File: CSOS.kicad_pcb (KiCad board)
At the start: 2 copper layers, 49.5 x 67.3 mm, 23 parts, among them P101 CONN_01X02, P102 CONN_01X03, P103 CONN_01X02, P201 CONN_01X01, Q201 BUK9575, U201 LMV358, U401 LM2931D-R

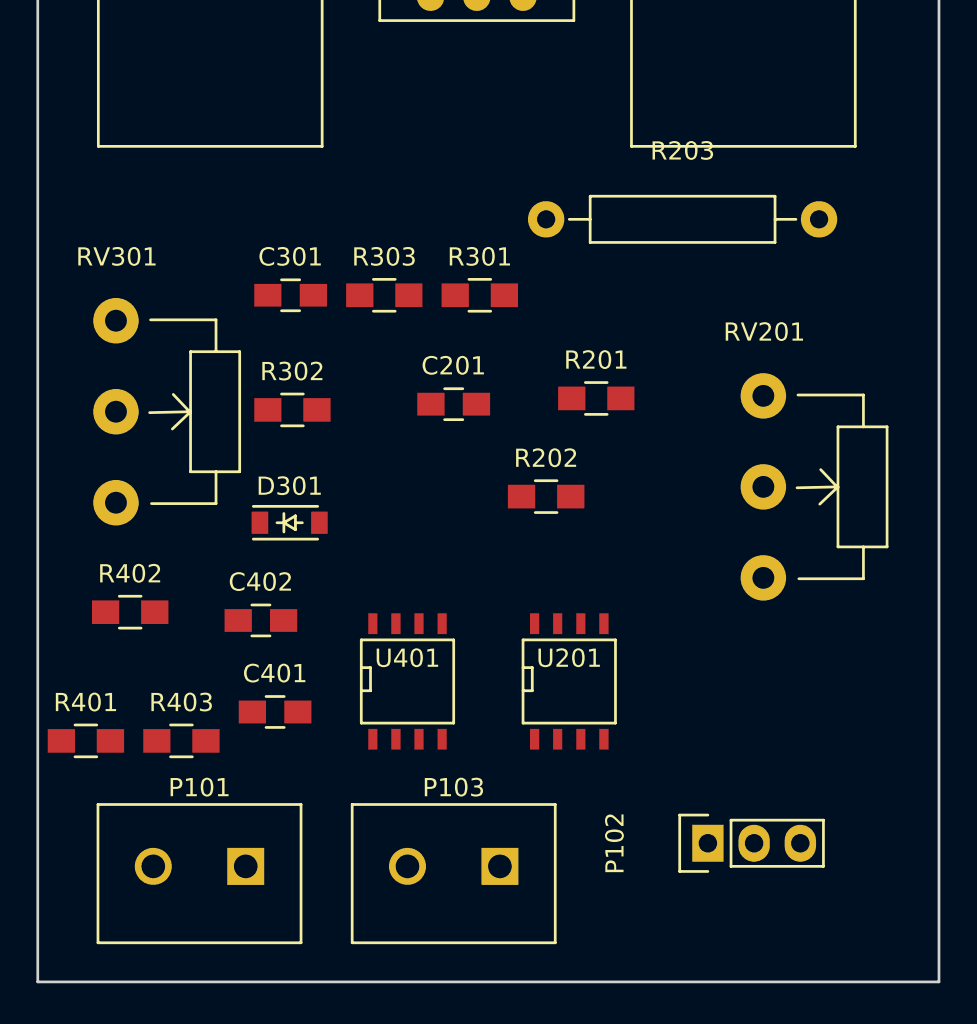
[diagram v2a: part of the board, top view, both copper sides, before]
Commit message: Built potentiometer and added to layout.
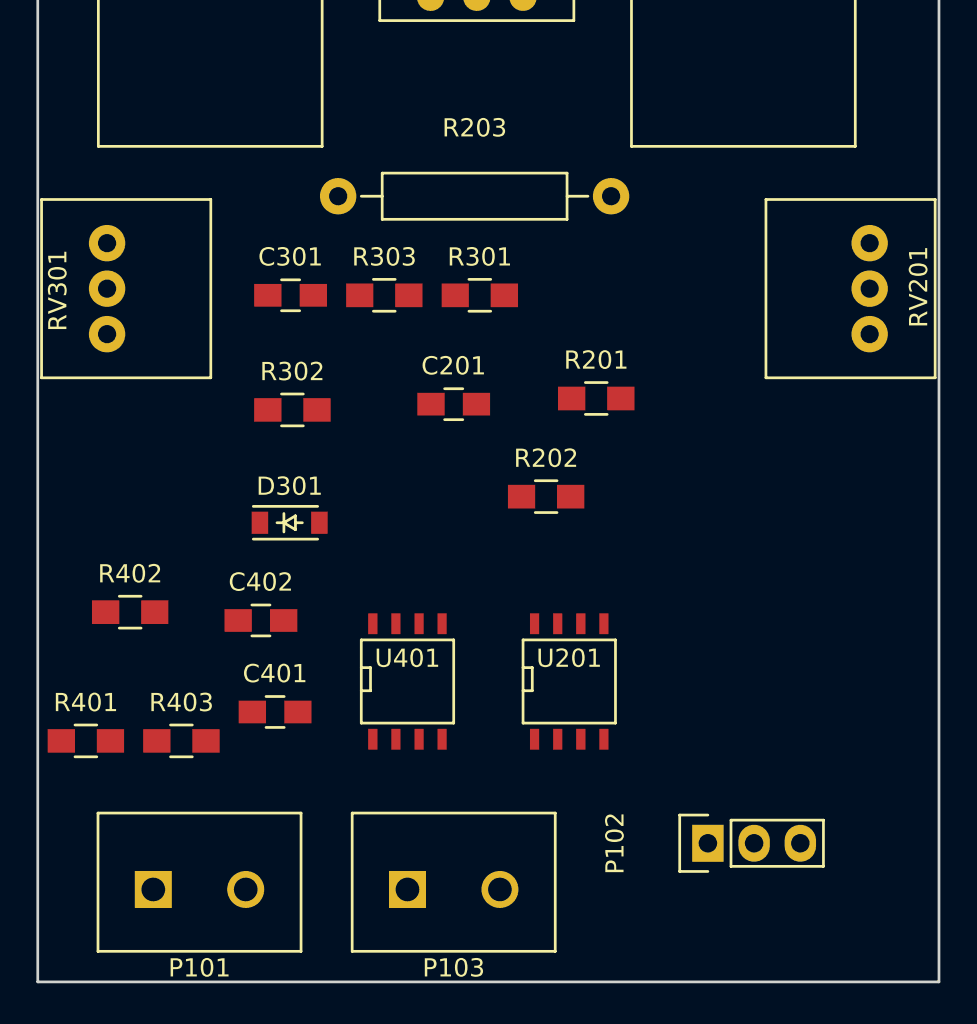
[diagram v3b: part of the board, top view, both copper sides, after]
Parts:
- RV201, RV301: footprint Potentiometers:Potentiometer_WirePads_largePads -> CSOS:P090L-02F25BR10K
- moved R203 11.5 mm to (139.7, 92.7)
- moved RV201 8.30 mm to (168.9, 97.8), turned to 90 degrees
- moved RV301 1.83 mm to (127.0, 97.8), turned to 270 degrees
- moved P101 1.27 mm to (132.1, 130.8), turned to 0 degrees
- moved P103 1.27 mm to (146.1, 130.8), turned to 0 degrees
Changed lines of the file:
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@@
   )
   (module Resistors_ThroughHole:Resistor_Horizontal_RM15mm (layer F.Cu)
-    (at 151.13 93.98)
+    (at 139.7 92.71)
     (descr "Resistor, Axial, RM 15mm,")
     (tags "Resistor Axial RM 15mm")
@@
       (rotate (xyz 0 0 0))
     )
-  )
-  (module Potentiometers:Potentiometer_WirePads_largePads (layer F.Cu)
-    (at 163.068502 103.68258)
-    (descr "Potentiometer, Wire Pads only, RevA, 30 July 2010,")
-    (tags "Potentiometer, Wire Pads only, RevA, 30 July 2010,")
-    (fp_text reference RV201 (at 0.0508 -3.49758) (layer F.SilkS)
-      (effects (font (size 1 1) (thickness 0.15)))
-    )
-    (fp_text value POT (at -1.34874 13.25118) (layer F.Fab)
-      (effects (font (size 1 1) (thickness 0.15)))
-    )
-    (fp_line (start 5.4991 10.05078) (end 1.95072 10.05078) (layer F.SilkS) (width 0.15))
-    (fp_line (start 5.4991 8.30072) (end 5.4991 10.05078) (layer F.SilkS) (width 0.15))
-    (fp_line (start 5.4991 1.7018) (end 5.4991 -0.04826) (layer F.SilkS) (width 0.15))
-    (fp_line (start 5.4991 -0.04826) (end 1.89992 -0.04826) (layer F.SilkS) (width 0.15))
-    (fp_line (start 4.09956 5.00126) (end 1.84912 5.05206) (layer F.SilkS) (width 0.15))
-    (fp_line (start 4.09956 5.00126) (end 3.0988 5.95122) (layer F.SilkS) (width 0.15))
-    (fp_line (start 4.09956 5.05206) (end 3.1496 4.0513) (layer F.SilkS) (width 0.15))
-    (fp_line (start 4.09956 1.7018) (end 6.79958 1.7018) (layer F.SilkS) (width 0.15))
-    (fp_line (start 6.79958 1.7018) (end 6.79958 8.30072) (layer F.SilkS) (width 0.15))
-    (fp_line (start 6.79958 8.30072) (end 4.09956 8.30072) (layer F.SilkS) (width 0.15))
-    (fp_line (start 4.09956 8.30072) (end 4.09956 1.7018) (layer F.SilkS) (width 0.15))
-    (pad 2 thru_hole circle (at 0 5.00126) (size 2.49936 2.49936) (drill 1.19888) (layers *.Cu *.Mask F.SilkS)
-      (net 1 2.7V))
-    (pad 3 thru_hole circle (at 0 10.00252) (size 2.49936 2.49936) (drill 1.19888) (layers *.Cu *.Mask F.SilkS)
-      (net 9 "Net-(R201-Pad1)"))
-    (pad 1 thru_hole circle (at 0 0) (size 2.49936 2.49936) (drill 1.19888) (layers *.Cu *.Mask F.SilkS)
-      (net 15 "Net-(RV201-Pad1)"))
-  )
-  (module Potentiometers:Potentiometer_WirePads_largePads (layer F.Cu)
-    (at 127.488502 99.55258)
-    (descr "Potentiometer, Wire Pads only, RevA, 30 July 2010,")
-    (tags "Potentiometer, Wire Pads only, RevA, 30 July 2010,")
-    (fp_text reference RV301 (at 0.0508 -3.49758) (layer F.SilkS)
-      (effects (font (size 1 1) (thickness 0.15)))
-    )
-    (fp_text value POT (at -1.34874 13.25118) (layer F.Fab)
-      (effects (font (size 1 1) (thickness 0.15)))
-    )
-    (fp_line (start 5.4991 10.05078) (end 1.95072 10.05078) (layer F.SilkS) (width 0.15))
-    (fp_line (start 5.4991 8.30072) (end 5.4991 10.05078) (layer F.SilkS) (width 0.15))
-    (fp_line (start 5.4991 1.7018) (end 5.4991 -0.04826) (layer F.SilkS) (width 0.15))
-    (fp_line (start 5.4991 -0.04826) (end 1.89992 -0.04826) (layer F.SilkS) (width 0.15))
-    (fp_line (start 4.09956 5.00126) (end 1.84912 5.05206) (layer F.SilkS) (width 0.15))
-    (fp_line (start 4.09956 5.00126) (end 3.0988 5.95122) (layer F.SilkS) (width 0.15))
-    (fp_line (start 4.09956 5.05206) (end 3.1496 4.0513) (layer F.SilkS) (width 0.15))
-    (fp_line (start 4.09956 1.7018) (end 6.79958 1.7018) (layer F.SilkS) (width 0.15))
-    (fp_line (start 6.79958 1.7018) (end 6.79958 8.30072) (layer F.SilkS) (width 0.15))
-    (fp_line (start 6.79958 8.30072) (end 4.09956 8.30072) (layer F.SilkS) (width 0.15))
-    (fp_line (start 4.09956 8.30072) (end 4.09956 1.7018) (layer F.SilkS) (width 0.15))
-    (pad 2 thru_hole circle (at 0 5.00126) (size 2.49936 2.49936) (drill 1.19888) (layers *.Cu *.Mask F.SilkS)
-      (net 1 2.7V))
-    (pad 3 thru_hole circle (at 0 10.00252) (size 2.49936 2.49936) (drill 1.19888) (layers *.Cu *.Mask F.SilkS)
-      (net 11 "Net-(R301-Pad1)"))
-    (pad 1 thru_hole circle (at 0 0) (size 2.49936 2.49936) (drill 1.19888) (layers *.Cu *.Mask F.SilkS)
-      (net 16 "Net-(RV301-Pad1)"))
   )
   (module SMD_Packages:SOIC-8-N (layer F.Cu)
@@
   )
   (module CSOS:Terminal_Block_200_mil (layer F.Cu)
-    (at 132.08 129.54 180)
+    (at 132.08 130.81)
     (descr "Through hole pin header")
     (tags "pin header")
-    (fp_text reference P101 (at 0 4.318 180) (layer F.SilkS)
-      (effects (font (size 1 1) (thickness 0.15)))
-    )
-    (fp_text value CONN_01X02 (at 0 -5.334 180) (layer F.Fab)
+    (fp_text reference P101 (at 0 4.318) (layer F.SilkS)
+      (effects (font (size 1 1) (thickness 0.15)))
+    )
+    (fp_text value CONN_01X02 (at 0 -5.334) (layer F.Fab)
       (effects (font (size 1 1) (thickness 0.15)))
     )
@@
     (fp_line (start -5.58 3.4) (end 5.58 3.4) (layer F.SilkS) (width 0.15))
     (fp_line (start -5.58 3.4) (end -5.58 -4.2) (layer F.SilkS) (width 0.15))
-    (pad 1 thru_hole rect (at -2.54 0) (size 2.032 2.032) (drill 1.3) (layers *.Cu *.Mask F.SilkS)
+    (pad 1 thru_hole rect (at -2.54 0 180) (size 2.032 2.032) (drill 1.3) (layers *.Cu *.Mask F.SilkS)
       (net 6 "Net-(P101-Pad1)"))
-    (pad 2 thru_hole oval (at 2.54 0) (size 2.032 2.032) (drill 1.3) (layers *.Cu *.Mask F.SilkS)
+    (pad 2 thru_hole oval (at 2.54 0 180) (size 2.032 2.032) (drill 1.3) (layers *.Cu *.Mask F.SilkS)
       (net 2 GND))
     (model Pin_Headers.3dshapes/Pin_Header_Straight_1x02.wrl
@@
   )
   (module CSOS:Terminal_Block_200_mil (layer F.Cu)
-    (at 146.05 129.54 180)
+    (at 146.05 130.81)
     (descr "Through hole pin header")
     (tags "pin header")
-    (fp_text reference P103 (at 0 4.318 180) (layer F.SilkS)
-      (effects (font (size 1 1) (thickness 0.15)))
-    )
-    (fp_text value CONN_01X02 (at 0 -5.334 180) (layer F.Fab)
+    (fp_text reference P103 (at 0 4.318) (layer F.SilkS)
+      (effects (font (size 1 1) (thickness 0.15)))
+    )
+    (fp_text value CONN_01X02 (at 0 -5.334) (layer F.Fab)
       (effects (font (size 1 1) (thickness 0.15)))
     )
@@
     (fp_line (start -5.58 3.4) (end 5.58 3.4) (layer F.SilkS) (width 0.15))
     (fp_line (start -5.58 3.4) (end -5.58 -4.2) (layer F.SilkS) (width 0.15))
-    (pad 1 thru_hole rect (at -2.54 0) (size 2.032 2.032) (drill 1.3) (layers *.Cu *.Mask F.SilkS)
+    (pad 1 thru_hole rect (at -2.54 0 180) (size 2.032 2.032) (drill 1.3) (layers *.Cu *.Mask F.SilkS)
       (net 7 "/Current Control/Current_Sink+"))
-    (pad 2 thru_hole oval (at 2.54 0) (size 2.032 2.032) (drill 1.3) (layers *.Cu *.Mask F.SilkS)
+    (pad 2 thru_hole oval (at 2.54 0 180) (size 2.032 2.032) (drill 1.3) (layers *.Cu *.Mask F.SilkS)
       (net 2 GND))
     (model Pin_Headers.3dshapes/Pin_Header_Straight_1x02.wrl
@@
     )
   )
+  (module CSOS:P090L-02F25BR10K (layer F.Cu)
+    (at 168.91 97.79 90)
+    (fp_text reference RV201 (at 0.1 2.7 90) (layer F.SilkS)
+      (effects (font (size 1 1) (thickness 0.15)))
+    )
+    (fp_text value POT (at 0 -6.7 90) (layer F.Fab)
+      (effects (font (size 1 1) (thickness 0.15)))
+    )
+    (fp_line (start -4.9 3.6) (end 4.9 3.6) (layer F.SilkS) (width 0.15))
+    (fp_line (start -4.9 -5.7) (end 4.9 -5.7) (layer F.SilkS) (width 0.15))
+    (fp_line (start 4.9 -5.7) (end 4.9 3.6) (layer F.SilkS) (width 0.15))
+    (fp_line (start -4.9 -5.7) (end -4.9 3.6) (layer F.SilkS) (width 0.15))
+    (pad "" np_thru_hole oval (at -5.1 -3.3 90) (size 2 2.2) (drill oval 2 2.2) (layers *.Cu *.Mask F.SilkS))
+    (pad 1 thru_hole circle (at -2.5 0 90) (size 2 2) (drill 1) (layers *.Cu *.Mask F.SilkS)
+      (net 15 "Net-(RV201-Pad1)"))
+    (pad 2 thru_hole circle (at 0 0 90) (size 2 2) (drill 1) (layers *.Cu *.Mask F.SilkS)
+      (net 1 2.7V))
+    (pad 3 thru_hole circle (at 2.5 0 90) (size 2 2) (drill 1) (layers *.Cu *.Mask F.SilkS)
+      (net 9 "Net-(R201-Pad1)"))
+    (pad "" np_thru_hole oval (at 5.1 -3.3 90) (size 2 2.2) (drill oval 2 2.2) (layers *.Cu *.Mask F.SilkS))
+  )
+  (module CSOS:P090L-02F25BR10K (layer F.Cu)
+    (at 127 97.79 270)
+    (fp_text reference RV301 (at 0.1 2.7 270) (layer F.SilkS)
+      (effects (font (size 1 1) (thickness 0.15)))
+    )
+    (fp_text value POT (at 0 -6.7 270) (layer F.Fab)
+      (effects (font (size 1 1) (thickness 0.15)))
+    )
+    (fp_line (start -4.9 3.6) (end 4.9 3.6) (layer F.SilkS) (width 0.15))
+    (fp_line (start -4.9 -5.7) (end 4.9 -5.7) (layer F.SilkS) (width 0.15))
+    (fp_line (start 4.9 -5.7) (end 4.9 3.6) (layer F.SilkS) (width 0.15))
+    (fp_line (start -4.9 -5.7) (end -4.9 3.6) (layer F.SilkS) (width 0.15))
+    (pad "" np_thru_hole oval (at -5.1 -3.3 270) (size 2 2.2) (drill oval 2 2.2) (layers *.Cu *.Mask F.SilkS))
+    (pad 1 thru_hole circle (at -2.5 0 270) (size 2 2) (drill 1) (layers *.Cu *.Mask F.SilkS)
+      (net 16 "Net-(RV301-Pad1)"))
+    (pad 2 thru_hole circle (at 0 0 270) (size 2 2) (drill 1) (layers *.Cu *.Mask F.SilkS)
+      (net 1 2.7V))
+    (pad 3 thru_hole circle (at 2.5 0 270) (size 2 2) (drill 1) (layers *.Cu *.Mask F.SilkS)
+      (net 11 "Net-(R301-Pad1)"))
+    (pad "" np_thru_hole oval (at 5.1 -3.3 270) (size 2 2.2) (drill oval 2 2.2) (layers *.Cu *.Mask F.SilkS))
+  )
   (gr_line (start 172.72 68.58) (end 172.72 135.89) (angle 90) (layer Edge.Cuts) (width 0.15))
